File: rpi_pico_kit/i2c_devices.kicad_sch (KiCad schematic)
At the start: 9 parts

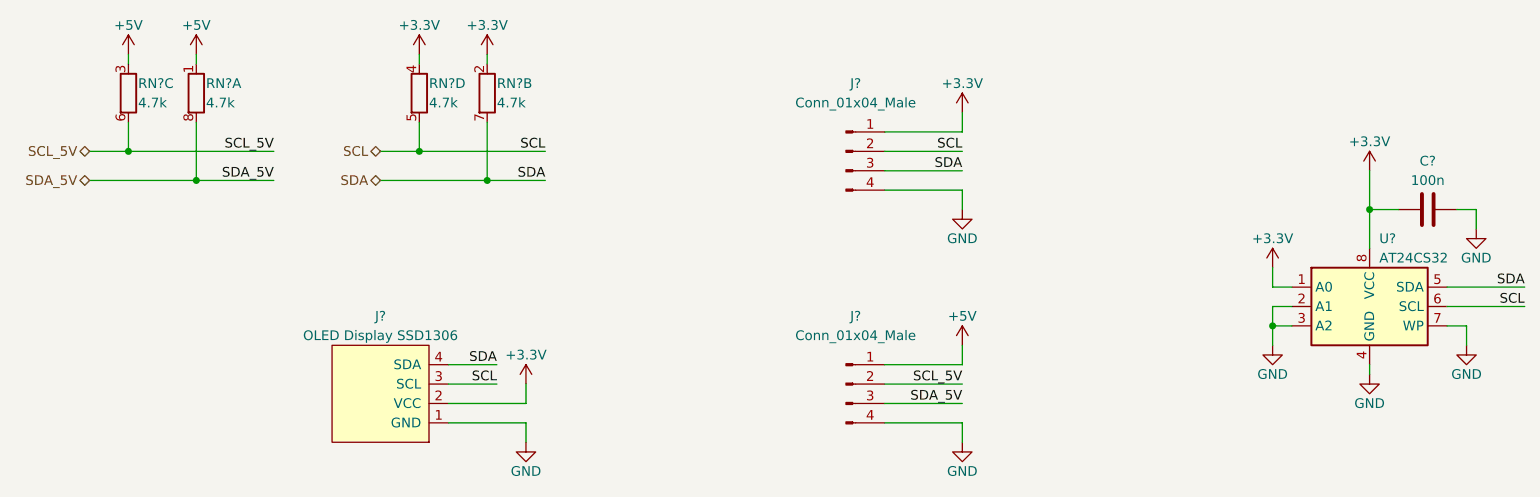
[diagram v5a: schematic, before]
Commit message: renumbered parts
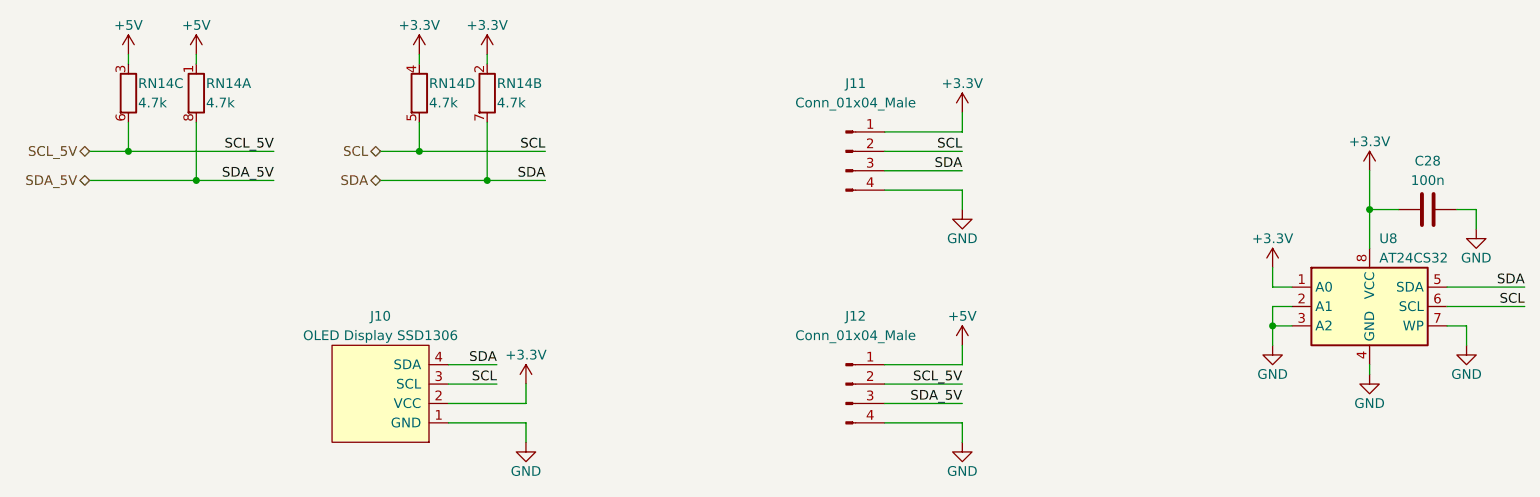
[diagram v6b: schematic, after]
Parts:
- gave numbers to parts that had none: 6
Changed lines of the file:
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@@
   (symbol (lib_id "Device:C") (at 227.33 83.82 90) (unit 1)
     (in_bom yes) (on_board yes)
-    (property "Reference" "C?" (id 0) (at 227.33 77.47 90)
+    (property "Reference" "C28" (id 0) (at 227.33 77.47 90)
       (effects (font (size 1.27 1.27)))
     )
@@
   (symbol (lib_id "Device:R_Pack04_Split") (at 95.25 68.58 180) (unit 4)
     (in_bom yes) (on_board yes)
-    (property "Reference" "RN?" (id 0) (at 96.52 67.31 0)
+    (property "Reference" "RN14" (id 0) (at 96.52 67.31 0)
       (effects (font (size 1.27 1.27)) (justify right))
     )
@@
   (symbol (lib_id "Device:R_Pack04_Split") (at 57.15 68.58 180) (unit 3)
     (in_bom yes) (on_board yes)
-    (property "Reference" "RN?" (id 0) (at 58.42 67.31 0)
+    (property "Reference" "RN14" (id 0) (at 58.42 67.31 0)
       (effects (font (size 1.27 1.27)) (justify right))
     )
@@
   (symbol (lib_id "Device:R_Pack04_Split") (at 104.14 68.58 180) (unit 2)
     (in_bom yes) (on_board yes)
-    (property "Reference" "RN?" (id 0) (at 105.41 67.31 0)
+    (property "Reference" "RN14" (id 0) (at 105.41 67.31 0)
       (effects (font (size 1.27 1.27)) (justify right))
     )
@@
   (symbol (lib_id "SSD1306:SSD1306") (at 90.17 107.95 270) (mirror x) (unit 1)
     (in_bom yes) (on_board yes) (fields_autoplaced)
-    (property "Reference" "J?" (id 0) (at 90.17 97.79 90)
+    (property "Reference" "J10" (id 0) (at 90.17 97.79 90)
       (effects (font (size 1.27 1.27)))
     )
@@
   (symbol (lib_id "Memory_EEPROM:AT24CS32-SSHM") (at 219.71 96.52 0) (unit 1)
     (in_bom yes) (on_board yes)
-    (property "Reference" "U?" (id 0) (at 220.98 87.63 0)
+    (property "Reference" "U8" (id 0) (at 220.98 87.63 0)
       (effects (font (size 1.27 1.27)) (justify left))
     )
@@
   (symbol (lib_id "Connector:Conn_01x04_Male") (at 151.13 76.2 0) (unit 1)
     (in_bom yes) (on_board yes)
-    (property "Reference" "J?" (id 0) (at 152.4 67.31 0)
+    (property "Reference" "J11" (id 0) (at 152.4 67.31 0)
       (effects (font (size 1.27 1.27)))
     )
@@
   (symbol (lib_id "Device:R_Pack04_Split") (at 66.04 68.58 180) (unit 1)
     (in_bom yes) (on_board yes)
-    (property "Reference" "RN?" (id 0) (at 67.31 67.31 0)
+    (property "Reference" "RN14" (id 0) (at 67.31 67.31 0)
       (effects (font (size 1.27 1.27)) (justify right))
     )
@@
   (symbol (lib_id "Connector:Conn_01x04_Male") (at 151.13 106.68 0) (unit 1)
     (in_bom yes) (on_board yes)
-    (property "Reference" "J?" (id 0) (at 152.4 97.79 0)
-      (effects (font (size 1.27 1.27)))
-    )
+    (property "Reference" "J12" (id 0) (at 152.4 97.79 0)
+      (effects (font (size 1.27 1.27)))
+    )
